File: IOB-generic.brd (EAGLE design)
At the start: 20.3 x 50.8 mm, 19 parts, among them J1 RJ12/6, Q0 P-FET, Q1 P-FET, Q2 P-FET, Q3 P-FET

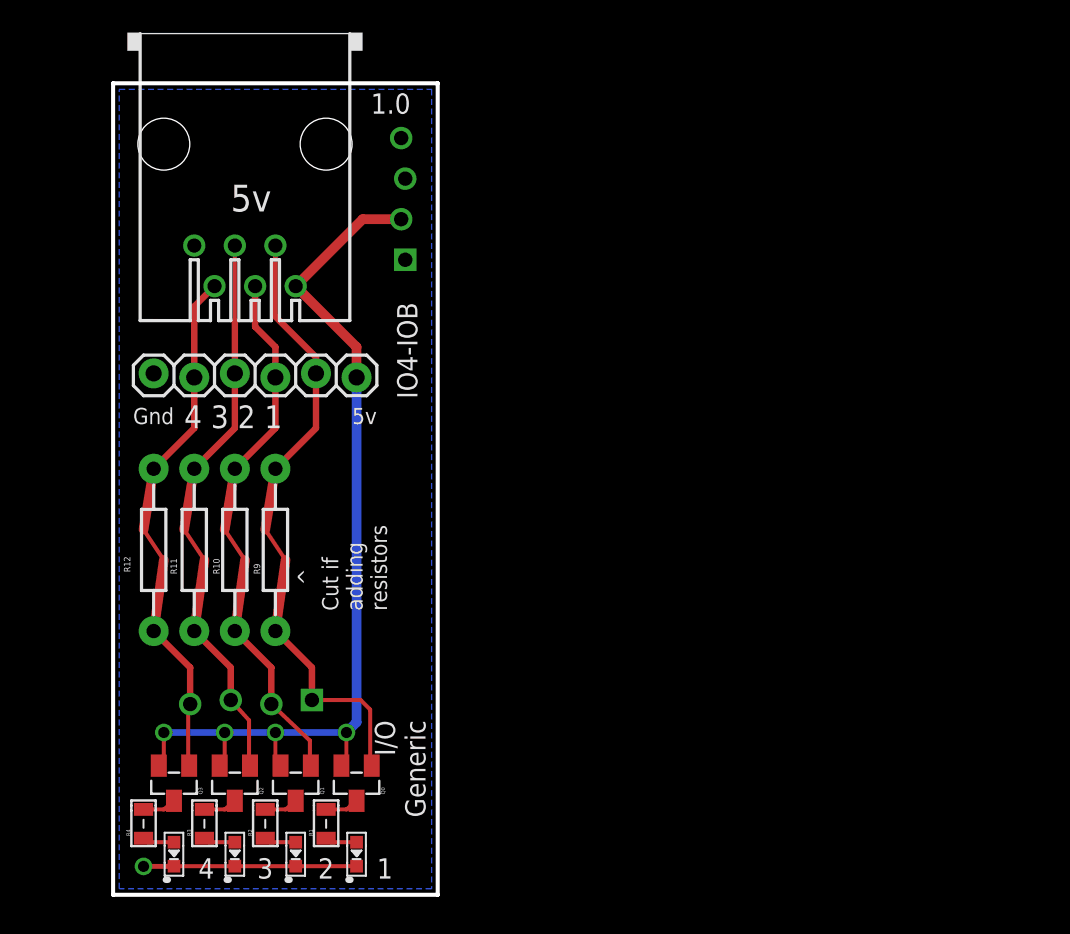
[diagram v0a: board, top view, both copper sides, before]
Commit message: NEW IOB form factor
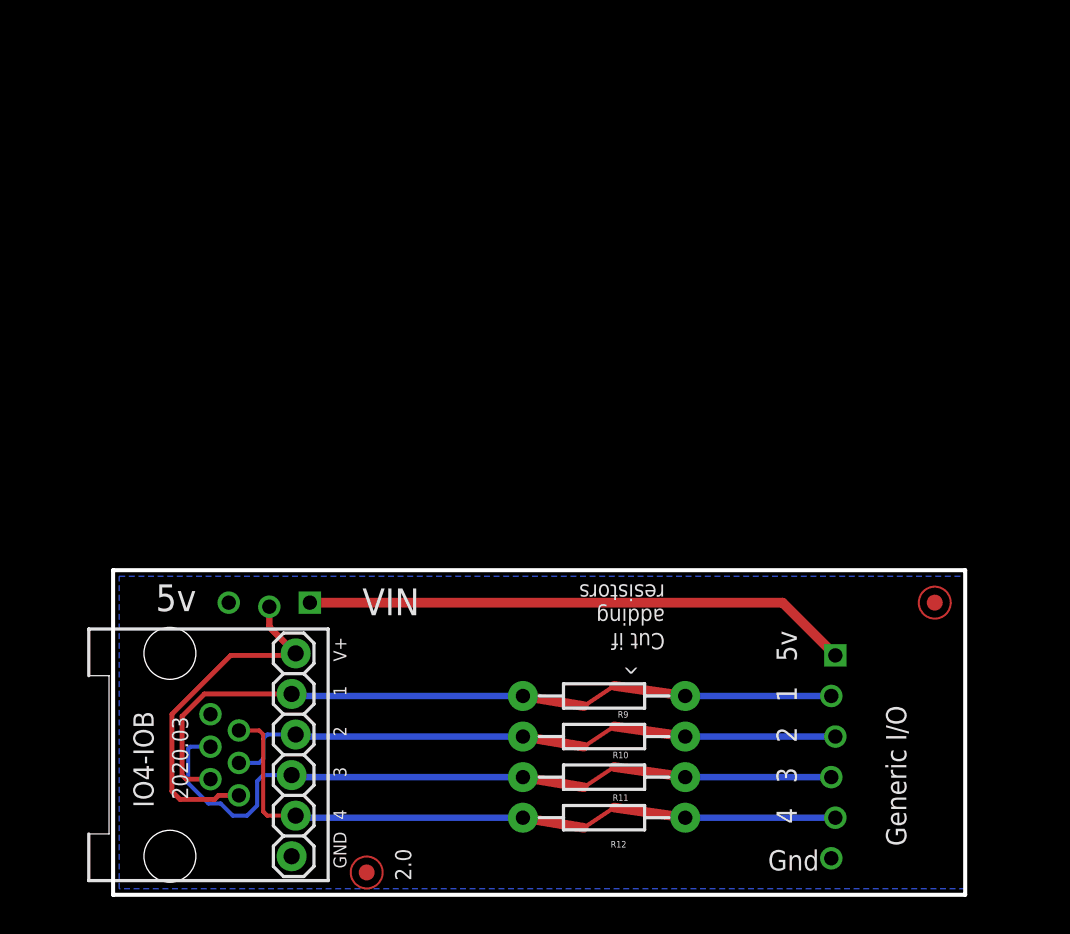
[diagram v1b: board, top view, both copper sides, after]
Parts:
- removed CON1: (no value), SPCoast:1X06_LOCK
- removed LED1, LED2, LED3, LED4: Y, SPCoast:0603-LED
- removed Q0, Q1, Q2, Q3: P-FET, SPCoast:SOT23
- removed R1, R2, R3, R4: 2K0, SPCoast:0805-RES
- added FID1, FID2: FIDUCIAL, SPCoast:FIDUCIAL_1MM
- J1: device SPCoast:RJ25-PANEL -> SPCoast:RJ24-INVERTED-PINS
- moved IOB 50.8 mm to (0.00, 0.00), turned to 0 degrees
- moved J1 38.2 mm to (7.37, 8.76), turned to 90 degrees
- moved R12 32.8 mm to (30.7, 4.83), turned to 180 degrees
- moved R11 29.3 mm to (30.7, 7.37), turned to 180 degrees
- moved R10 25.9 mm to (30.7, 9.91), turned to 180 degrees
- moved R9 22.5 mm to (30.7, 12.4), turned to 180 degrees
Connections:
- removed net N$11: Q0.3, R1.2
- removed net N$2: LED1.A, R1.1
- removed net N$3: LED2.A, R2.1
- removed net N$30: Q1.3, R2.2
- removed net N$31: Q2.3, R3.2
- removed net N$32: Q3.3, R4.2
- removed net N$4: LED3.A, R3.1
- removed net N$5: LED4.A, R4.1
- new net VOUT: IOB.VOUT, J1.1, J1.1@1
- net !IO1: now also J1.2@1; no longer CON1.2
- net !IO2: now also J1.3@1; no longer CON1.3
- net !IO3: now also J1.4@1; no longer CON1.4
- net !IO4: now also J1.5@1; no longer CON1.5
- net GND: now also IOB.G@3, J1.6@1; no longer CON1.6, IOB.G@1, IOB.G@2, LED1.C, LED2.C, LED3.C, LED4.C
- net P1: no longer Q0.1
- net P2: no longer Q1.1
- net P3: no longer Q2.1
- net P4: no longer Q3.1
- net VCC: now also IOB.V5@1; no longer CON1.1, J1.1, Q0.2, Q1.2, Q2.2, Q3.2
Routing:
- net VCC: track 58.7 -> 34.3 mm, vias 4 -> 0
- net VOUT: track 0.00 -> 22.3 mm
- net GND: track 13.3 -> 0.00 mm, vias 1 -> 0
- net !IO3: track 21.2 -> 33.6 mm, vias 0 -> 1
- net !IO1: track 22.2 -> 33.7 mm, vias 0 -> 1
- net !IO4: track 19.2 -> 29.0 mm, vias 0 -> 1
- net !IO2: track 19.2 -> 25.5 mm, vias 0 -> 1
- net P1: track 17.3 -> 13.6 mm
- net N$31: track 2.11 -> 0.00 mm
- net N$32: track 2.11 -> 0.00 mm
- net N$30: track 2.11 -> 0.00 mm
- net N$11: track 2.11 -> 0.00 mm
- net N$4: track 2.01 -> 0.00 mm
- net N$5: track 2.01 -> 0.00 mm
- net N$3: track 2.01 -> 0.00 mm
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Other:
- board size 20.3 x 50.8 mm -> 53.3 x 20.3 mm
- board text added: "2.0"
- board text added: "2020.03"
- board text added: "Generic I/O"
- board text added: "Generic Quad I/O"
- board text removed: "1"
- board text removed: "1.0"
- board text removed: "2"
- board text removed: "3"
- board text removed: "4"
- board text removed: "4 3 2 1"
- board text removed: "5v"
- board text removed: "Gnd"
- board text removed: "I/O Generic"
- board text removed: "IOB to IO4 Interface"
- board text removed: "Made in the PCR, Coast Div, NMRA"
- board text removed: "Model Railroading is Fun!"
- board text removed: "Q0"
- board text removed: "Q1"
- board text removed: "Q2"
- board text removed: "Q3"
- board text removed: "Quad I/O"
- board text removed: "R1"
- board text removed: "R2"
- board text removed: "R3"
- board text removed: "R4"

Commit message: generated new array
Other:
- board text removed: "R10"
- board text removed: "R11"
- board text removed: "R12"
- board text removed: "R9"
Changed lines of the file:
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@@
 <layer number="60" name="bCarbon" color="7" fill="1" visible="no" active="no"/>
 <layer number="90" name="Modules" color="5" fill="1" visible="no" active="no"/>
-<layer number="100" name="Muster" color="7" fill="1" visible="no" active="no"/>
-<layer number="101" name="Hidden" color="57" fill="4" visible="yes" active="yes"/>
-<layer number="102" name="Changes" color="13" fill="1" visible="yes" active="yes"/>
-<layer number="103" name="tMap" color="29" fill="4" visible="no" active="yes"/>
-<layer number="104" name="Name" color="16" fill="1" visible="yes" active="yes"/>
-<layer number="105" name="tPlate" color="7" fill="1" visible="no" active="yes"/>
-<layer number="106" name="bPlate" color="7" fill="1" visible="no" active="yes"/>
-<layer number="107" name="Crop" color="7" fill="1" visible="no" active="yes"/>
-<layer number="108" name="fp8" color="7" fill="1" visible="no" active="yes"/>
-<layer number="109" name="fp9" color="7" fill="1" visible="no" active="yes"/>
-<layer number="110" name="fp0" color="7" fill="1" visible="no" active="yes"/>
-<layer number="111" name="bdokum" color="7" fill="1" visible="no" active="yes"/>
-<layer number="112" name="tSilk" color="7" fill="1" visible="no" active="no"/>
-<layer number="113" name="IDFDebug" color="7" fill="1" visible="no" active="yes"/>
-<layer number="114" name="Rect_Pads" color="7" fill="1" visible="no" active="yes"/>
-<layer number="115" name="_tsilk" color="7" fill="1" visible="no" active="yes"/>
-<layer number="116" name="Patch_BOT" color="9" fill="4" visible="no" active="yes"/>
-<layer number="117" name="tTestmark" color="7" fill="1" visible="no" active="yes"/>
-<layer number="118" name="Rect_Pads" color="7" fill="1" visible="no" active="no"/>
-<layer number="119" name="_tNames" color="7" fill="1" visible="no" active="yes"/>
-<layer number="120" name="_bNames" color="7" fill="1" visible="no" active="yes"/>
-<layer number="121" name="_tsilk" color="7" fill="1" visible="no" active="yes"/>
-<layer number="122" name="_bsilk" color="7" fill="1" visible="no" active="yes"/>
-<layer number="123" name="tTestmark" color="7" fill="1" visible="no" active="yes"/>
-<layer number="124" name="bTestmark" color="7" fill="1" visible="no" active="yes"/>
-<layer number="125" name="_tNames" color="14" fill="1" visible="no" active="yes"/>
-<layer number="126" name="_bNames" color="7" fill="1" visible="no" active="yes"/>
-<layer number="127" name="_tValues" color="7" fill="1" visible="no" active="no"/>
-<layer number="128" name="_bValues" color="7" fill="1" visible="no" active="no"/>
-<layer number="129" name="Mask" color="7" fill="1" visible="no" active="yes"/>
-<layer number="130" name="SMDSTROOK" color="7" fill="1" visible="no" active="yes"/>
-<layer number="131" name="tAdjust" color="7" fill="1" visible="no" active="yes"/>
-<layer number="132" name="bAdjust" color="7" fill="1" visible="no" active="yes"/>
-<layer number="144" name="Drill_legend" color="7" fill="1" visible="no" active="yes"/>
-<layer number="146" name="Housing" color="7" fill="1" visible="no" active="yes"/>
-<layer number="147" name="Edge" color="7" fill="1" visible="no" active="yes"/>
-<layer number="148" name="ReferenceLC" color="7" fill="1" visible="no" active="yes"/>
-<layer number="149" name="ReferenceLS" color="7" fill="1" visible="no" active="yes"/>
-<layer number="150" name="Notes" color="7" fill="1" visible="no" active="yes"/>
-<layer number="151" name="HeatSink" color="7" fill="1" visible="no" active="yes"/>
-<layer number="152" name="_bDocu" color="7" fill="1" visible="no" active="no"/>
-<layer number="153" name="FabDoc1" color="7" fill="1" visible="no" active="yes"/>
-<layer number="154" name="FabDoc2" color="7" fill="1" visible="no" active="yes"/>
-<layer number="155" name="FabDoc3" color="7" fill="1" visible="no" active="yes"/>
-<layer number="199" name="Contour" color="7" fill="1" visible="no" active="yes"/>
-<layer number="200" name="200bmp" color="1" fill="10" visible="no" active="yes"/>
-<layer number="201" name="201bmp" color="2" fill="10" visible="no" active="yes"/>
-<layer number="202" name="202bmp" color="3" fill="10" visible="no" active="yes"/>
-<layer number="203" name="203bmp" color="4" fill="10" visible="no" active="yes"/>
-<layer number="204" name="204bmp" color="5" fill="10" visible="no" active="yes"/>
-<layer number="205" name="205bmp" color="6" fill="10" visible="no" active="yes"/>
-<layer number="206" name="206bmp" color="7" fill="10" visible="no" active="yes"/>
-<layer number="207" name="207bmp" color="8" fill="10" visible="no" active="yes"/>
-<layer number="208" name="208bmp" color="9" fill="10" visible="no" active="yes"/>
-<layer number="209" name="209bmp" color="7" fill="1" visible="no" active="yes"/>
-<layer number="210" name="210bmp" color="7" fill="1" visible="no" active="yes"/>
-<layer number="211" name="211bmp" color="12" fill="1" visible="no" active="no"/>
-<layer number="212" name="212bmp" color="13" fill="1" visible="no" active="no"/>
-<layer number="213" name="213bmp" color="14" fill="1" visible="no" active="no"/>
-<layer number="214" name="214bmp" color="15" fill="1" visible="no" active="no"/>
-<layer number="215" name="215bmp" color="16" fill="1" visible="no" active="no"/>
-<layer number="216" name="216bmp" color="17" fill="1" visible="no" active="no"/>
-<layer number="217" name="217bmp" color="18" fill="1" visible="no" active="no"/>
-<layer number="218" name="218bmp" color="19" fill="1" visible="no" active="no"/>
-<layer number="219" name="219bmp" color="20" fill="1" visible="no" active="no"/>
-<layer number="220" name="220bmp" color="21" fill="1" visible="no" active="no"/>
-<layer number="221" name="221bmp" color="22" fill="1" visible="no" active="no"/>
-<layer number="222" name="222bmp" color="23" fill="1" visible="no" active="no"/>
-<layer number="223" name="223bmp" color="24" fill="1" visible="no" active="no"/>
-<layer number="224" name="224bmp" color="25" fill="1" visible="no" active="no"/>
-<layer number="225" name="225bmp" color="7" fill="1" visible="no" active="yes"/>
-<layer number="226" name="226bmp" color="7" fill="1" visible="no" active="yes"/>
-<layer number="227" name="227bmp" color="7" fill="1" visible="no" active="yes"/>
-<layer number="228" name="228bmp" color="7" fill="1" visible="no" active="yes"/>
-<layer number="229" name="229bmp" color="7" fill="1" visible="no" active="yes"/>
-<layer number="230" name="230bmp" color="7" fill="1" visible="no" active="yes"/>
-<layer number="231" name="231bmp" color="7" fill="1" visible="no" active="yes"/>
-<layer number="232" name="Eagle3D_PG2" color="7" fill="1" visible="no" active="yes"/>
-<layer number="233" name="Eagle3D_PG3" color="7" fill="1" visible="no" active="yes"/>
-<layer number="247" name="wrappinf" color="7" fill="1" visible="no" active="yes"/>
-<layer number="248" name="Housing" color="7" fill="1" visible="no" active="no"/>
-<layer number="249" name="Edge" color="7" fill="1" visible="no" active="no"/>
-<layer number="250" name="Descript" color="3" fill="1" visible="no" active="no"/>
-<layer number="251" name="SMDround" color="12" fill="11" visible="no" active="no"/>
-<layer number="252" name="BR-BS" color="7" fill="1" visible="no" active="yes"/>
-<layer number="253" name="BR-LS" color="7" fill="1" visible="no" active="yes"/>
-<layer number="254" name="cooling" color="7" fill="1" visible="no" active="yes"/>
-<layer number="255" name="routoute" color="7" fill="1" visible="no" active="yes"/>
 </layers>
 <board>
@@
 adding
 resistors</text>
-<text x="32.258" y="11.4935" size="0.4064" layer="125" font="vector" rot="R180">R9</text>
-<text x="32.258" y="8.9535" size="0.4064" layer="125" font="vector" rot="R180">R10</text>
-<text x="32.258" y="6.2865" size="0.4064" layer="125" font="vector" rot="R180">R11</text>
-<text x="30.607" y="1.0795" size="0.4064" layer="125" font="vector" rot="R180">R12</text>
 <text x="4.699" y="5.969" size="1.016" layer="21" font="vector" rot="R90">2020.03</text>
 </plain>

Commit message: silkscreen and top fill
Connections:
- removed net VCC: IOB.V5, IOB.V5@1
- new net VIN: IOB.V+
- net VCCIO: now also IOB.V5, IOB.V5@1; no longer IOB.V+
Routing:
- net VCC: track 34.3 -> 0.00 mm
- added copper zone on layer 1, net VCCIO
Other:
- board text added: "2.1"
- board text added: "Cut if < using resistor"
- board text added: "Yellow Headers"
- board text removed: "2.0"
- board text removed: "^ Cut if adding resistors"
